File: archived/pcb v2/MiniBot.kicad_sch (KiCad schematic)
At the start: 42 parts, among them IC1 MMC5633NJL, IC2 MIC23050-SYML-TR, J1 Conn_01x08, J2 Conn_01x02, J3 GSB1C41110SSHR, J4 Conn_01x01, U1 ESP32-C3-MINI-1-H4X, U3 MCP73832-2-OT

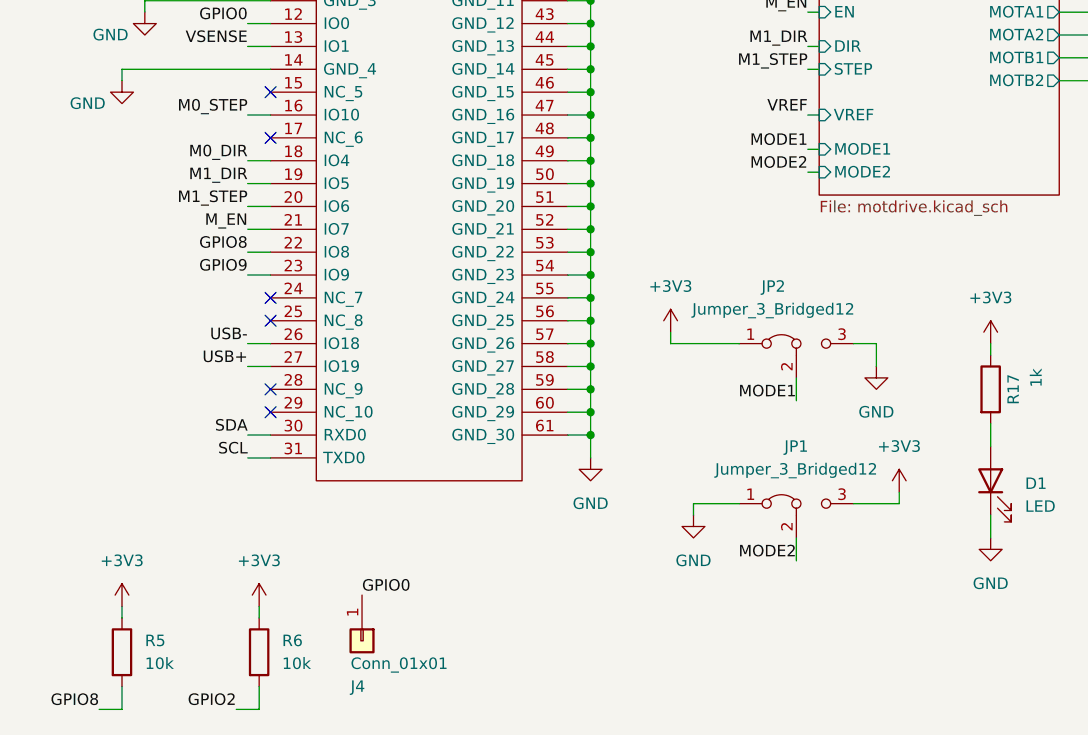
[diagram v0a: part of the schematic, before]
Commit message: reorg and write device ID to NVS
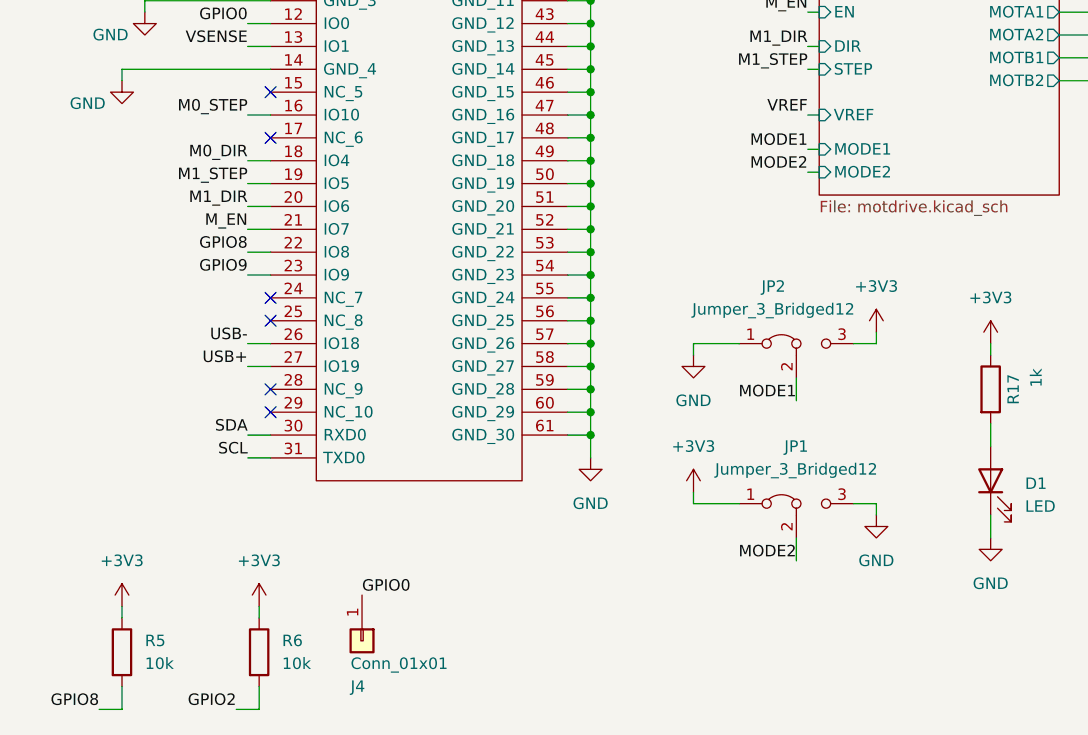
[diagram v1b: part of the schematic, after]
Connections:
- net +3V3: now also JP1.1 (A), JP2.3 (B); no longer JP1.3 (B), JP2.1 (A)
- net GND: now also JP1.3 (B), JP2.1 (A); no longer JP1.1 (A), JP2.3 (B)
- net M1_DIR: now also U1.20 (IO6); no longer U1.19 (IO5)
- net M1_STEP: now also U1.19 (IO5); no longer U1.20 (IO6)
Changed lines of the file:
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@@
     (stroke (width 0) (type default))
   )
-  (wire (pts (xy 107.95 96.52) (xy 100.33 96.52))
+  (wire (pts (xy 107.95 96.52) (xy 102.87 96.52))
     (stroke (width 0) (type default))
   )
@@
     (stroke (width 0) (type default))
   )
+  (wire (pts (xy 102.87 96.52) (xy 102.87 97.79))
+    (stroke (width 0) (type default))
+  )
   (wire (pts (xy 271.78 59.69) (xy 274.32 59.69))
     (stroke (width 0) (type default))
@@
     (stroke (width 0) (type default))
   )
-  (wire (pts (xy 102.87 114.3) (xy 102.87 115.57))
-    (stroke (width 0) (type default))
-  )
   (wire (pts (xy 91.44 106.68) (xy 91.44 109.22))
     (stroke (width 0) (type default))
   )
-  (wire (pts (xy 123.19 96.52) (xy 123.19 99.06))
-    (stroke (width 0) (type default))
-  )
   (wire (pts (xy 88.9 60.96) (xy 91.44 60.96))
     (stroke (width 0) (type default))
@@
     (stroke (width 0) (type default))
   )
+  (wire (pts (xy 123.19 114.3) (xy 123.19 115.57))
+    (stroke (width 0) (type default))
+  )
   (wire (pts (xy 91.44 93.98) (xy 91.44 96.52))
     (stroke (width 0) (type default))
@@
     (stroke (width 0) (type default))
   )
+  (wire (pts (xy 102.87 114.3) (xy 102.87 113.03))
+    (stroke (width 0) (type default))
+  )
+  (wire (pts (xy 123.19 95.25) (xy 123.19 96.52))
+    (stroke (width 0) (type default))
+  )
   (wire (pts (xy 250.19 30.48) (xy 251.46 30.48))
     (stroke (width 0) (type default))
@@
     (stroke (width 0) (type default))
   )
-  (wire (pts (xy 120.65 114.3) (xy 125.73 114.3))
+  (wire (pts (xy 120.65 114.3) (xy 123.19 114.3))
     (stroke (width 0) (type default))
   )
@@
     (stroke (width 0) (type default))
   )
-  (wire (pts (xy 125.73 113.03) (xy 125.73 114.3))
-    (stroke (width 0) (type default))
-  )
   (wire (pts (xy 54.61 33.02) (xy 48.26 33.02))
     (stroke (width 0) (type default))
@@
   )
   (wire (pts (xy 48.26 33.02) (xy 48.26 36.83))
-    (stroke (width 0) (type default))
-  )
-  (wire (pts (xy 100.33 95.25) (xy 100.33 96.52))
     (stroke (width 0) (type default))
   )
@@
     (effects (font (size 1.27 1.27)) (justify right bottom))
   )
-  (label "M1_DIR" (at 53.34 78.74 180) (fields_autoplaced)
+  (label "M1_STEP" (at 53.34 78.74 180) (fields_autoplaced)
     (effects (font (size 1.27 1.27)) (justify right bottom))
   )
@@
   )
   (label "M0_DIR" (at 53.34 76.2 180) (fields_autoplaced)
+    (effects (font (size 1.27 1.27)) (justify right bottom))
+  )
+  (label "M1_DIR" (at 53.34 81.28 180) (fields_autoplaced)
     (effects (font (size 1.27 1.27)) (justify right bottom))
   )
@@
   )
   (label "CFF" (at 204.47 41.91 180) (fields_autoplaced)
-    (effects (font (size 1.27 1.27)) (justify right bottom))
-  )
-  (label "M1_STEP" (at 53.34 81.28 180) (fields_autoplaced)
     (effects (font (size 1.27 1.27)) (justify right bottom))
   )
@@
     )
   )
-  (symbol (lib_id "power:GND") (at 123.19 99.06 0) (unit 1)
-    (in_bom yes) (on_board yes) (dnp no) (fields_autoplaced)
-    (property "Reference" "#PWR038" (at 123.19 105.41 0)
-      (effects (font (size 1.27 1.27)) hide)
-    )
-    (property "Value" "GND" (at 123.19 104.14 0)
-      (effects (font (size 1.27 1.27)))
-    )
-    (property "Footprint" "" (at 123.19 99.06 0)
-      (effects (font (size 1.27 1.27)) hide)
-    )
-    (property "Datasheet" "" (at 123.19 99.06 0)
-      (effects (font (size 1.27 1.27)) hide)
-    )
-    (pin "1")
-    (instances
-      (project "MiniBot"
-        (path "/0e598331-3211-4e8a-a305-31a83585854d"
-          (reference "#PWR038") (unit 1)
-        )
-      )
-    )
-  )
   (symbol (lib_id "power:VDC") (at 245.11 62.23 90) (unit 1)
     (in_bom yes) (on_board yes) (dnp no) (fields_autoplaced)
@@
     )
   )
+  (symbol (lib_id "power:+3V3") (at 123.19 95.25 0) (unit 1)
+    (in_bom yes) (on_board yes) (dnp no) (fields_autoplaced)
+    (property "Reference" "#PWR056" (at 123.19 99.06 0)
+      (effects (font (size 1.27 1.27)) hide)
+    )
+    (property "Value" "+3V3" (at 123.19 90.17 0)
+      (effects (font (size 1.27 1.27)))
+    )
+    (property "Footprint" "" (at 123.19 95.25 0)
+      (effects (font (size 1.27 1.27)) hide)
+    )
+    (property "Datasheet" "" (at 123.19 95.25 0)
+      (effects (font (size 1.27 1.27)) hide)
+    )
+    (pin "1")
+    (instances
+      (project "MiniBot"
+        (path "/0e598331-3211-4e8a-a305-31a83585854d"
+          (reference "#PWR056") (unit 1)
+        )
+      )
+    )
+  )
   (symbol (lib_id "power:+3V3") (at 54.61 180.34 0) (unit 1)
     (in_bom yes) (on_board yes) (dnp no) (fields_autoplaced)
@@
         (path "/0e598331-3211-4e8a-a305-31a83585854d"
           (reference "D1") (unit 1)
-        )
-      )
-    )
-  )
-  (symbol (lib_id "power:GND") (at 102.87 115.57 0) (unit 1)
-    (in_bom yes) (on_board yes) (dnp no) (fields_autoplaced)
-    (property "Reference" "#PWR057" (at 102.87 121.92 0)
-      (effects (font (size 1.27 1.27)) hide)
-    )
-    (property "Value" "GND" (at 102.87 120.65 0)
-      (effects (font (size 1.27 1.27)))
-    )
-    (property "Footprint" "" (at 102.87 115.57 0)
-      (effects (font (size 1.27 1.27)) hide)
-    )
-    (property "Datasheet" "" (at 102.87 115.57 0)
-      (effects (font (size 1.27 1.27)) hide)
-    )
-    (pin "1")
-    (instances
-      (project "MiniBot"
-        (path "/0e598331-3211-4e8a-a305-31a83585854d"
-          (reference "#PWR057") (unit 1)
         )
       )
@@
     )
   )
-  (symbol (lib_id "power:+3V3") (at 125.73 113.03 0) (unit 1)
-    (in_bom yes) (on_board yes) (dnp no) (fields_autoplaced)
-    (property "Reference" "#PWR067" (at 125.73 116.84 0)
-      (effects (font (size 1.27 1.27)) hide)
-    )
-    (property "Value" "+3V3" (at 125.73 107.95 0)
-      (effects (font (size 1.27 1.27)))
-    )
-    (property "Footprint" "" (at 125.73 113.03 0)
-      (effects (font (size 1.27 1.27)) hide)
-    )
-    (property "Datasheet" "" (at 125.73 113.03 0)
-      (effects (font (size 1.27 1.27)) hide)
-    )
-    (pin "1")
-    (instances
-      (project "MiniBot"
-        (path "/0e598331-3211-4e8a-a305-31a83585854d"
-          (reference "#PWR067") (unit 1)
-        )
-      )
-    )
-  )
   (symbol (lib_id "power:GND") (at 91.44 109.22 0) (unit 1)
     (in_bom yes) (on_board yes) (dnp no) (fields_autoplaced)
@@
         (path "/0e598331-3211-4e8a-a305-31a83585854d"
           (reference "#PWR018") (unit 1)
+        )
+      )
+    )
+  )
+  (symbol (lib_id "power:GND") (at 123.19 115.57 0) (unit 1)
+    (in_bom yes) (on_board yes) (dnp no) (fields_autoplaced)
+    (property "Reference" "#PWR047" (at 123.19 121.92 0)
+      (effects (font (size 1.27 1.27)) hide)
+    )
+    (property "Value" "GND" (at 123.19 120.65 0)
+      (effects (font (size 1.27 1.27)))
+    )
+    (property "Footprint" "" (at 123.19 115.57 0)
+      (effects (font (size 1.27 1.27)) hide)
+    )
+    (property "Datasheet" "" (at 123.19 115.57 0)
+      (effects (font (size 1.27 1.27)) hide)
+    )
+    (pin "1")
+    (instances
+      (project "MiniBot"
+        (path "/0e598331-3211-4e8a-a305-31a83585854d"
+          (reference "#PWR047") (unit 1)
         )
       )
@@
     )
   )
+  (symbol (lib_id "power:+3V3") (at 102.87 113.03 0) (unit 1)
+    (in_bom yes) (on_board yes) (dnp no) (fields_autoplaced)
+    (property "Reference" "#PWR050" (at 102.87 116.84 0)
+      (effects (font (size 1.27 1.27)) hide)
+    )
+    (property "Value" "+3V3" (at 102.87 107.95 0)
+      (effects (font (size 1.27 1.27)))
+    )
+    (property "Footprint" "" (at 102.87 113.03 0)
+      (effects (font (size 1.27 1.27)) hide)
+    )
+    (property "Datasheet" "" (at 102.87 113.03 0)
+      (effects (font (size 1.27 1.27)) hide)
+    )
+    (pin "1")
+    (instances
+      (project "MiniBot"
+        (path "/0e598331-3211-4e8a-a305-31a83585854d"
+          (reference "#PWR050") (unit 1)
+        )
+      )
+    )
+  )
   (symbol (lib_id "power:GND") (at 156.21 119.38 0) (unit 1)
     (in_bom yes) (on_board yes) (dnp no) (fields_autoplaced)
@@
         (path "/0e598331-3211-4e8a-a305-31a83585854d"
           (reference "#PWR042") (unit 1)
+        )
+      )
+    )
+  )
+  (symbol (lib_id "power:GND") (at 102.87 97.79 0) (unit 1)
+    (in_bom yes) (on_board yes) (dnp no) (fields_autoplaced)
+    (property "Reference" "#PWR045" (at 102.87 104.14 0)
+      (effects (font (size 1.27 1.27)) hide)
+    )
+    (property "Value" "GND" (at 102.87 102.87 0)
+      (effects (font (size 1.27 1.27)))
+    )
+    (property "Footprint" "" (at 102.87 97.79 0)
+      (effects (font (size 1.27 1.27)) hide)
+    )
+    (property "Datasheet" "" (at 102.87 97.79 0)
+      (effects (font (size 1.27 1.27)) hide)
+    )
+    (pin "1")
+    (instances
+      (project "MiniBot"
+        (path "/0e598331-3211-4e8a-a305-31a83585854d"
+          (reference "#PWR045") (unit 1)
         )
       )
@@
         )
       )
-    )
-  )
-  (symbol (lib_id "power:+3V3") (at 100.33 95.25 0) (unit 1)
-    (in_bom yes) (on_board yes) (dnp no) (fields_autoplaced)
-    (property "Reference" "#PWR037" (at 100.33 99.06 0)
-      (effects (font (size 1.27 1.27)) hide)
-    )
-    (property "Value" "+3V3" (at 100.33 90.17 0)
-      (effects (font (size 1.27 1.27)))
-    )
-    (property "Footprint" "" (at 100.33 95.25 0)
-      (effects (font (size 1.27 1.27)) hide)
-    )
-    (property "Datasheet" "" (at 100.33 95.25 0)
-      (effects (font (size 1.27 1.27)) hide)
-    )
-    (pin "1")
-    (instances
-      (project "MiniBot"
-        (path "/0e598331-3211-4e8a-a305-31a83585854d"
-          (reference "#PWR037") (unit 1)
-        )
-      )
